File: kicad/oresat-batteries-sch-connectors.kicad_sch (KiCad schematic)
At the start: 13 parts, among them J1 J-SAMTEC-TFM-120-X1-XXX-D-RA, SW1 Omron D2F-L3-D (LEFT), SW2 Omron D2F-L3-D (RIGHT), SW3 OMRON D2F-L3-D (LEFT), SW4 OMRON D2F-L3-D (RIGHT)

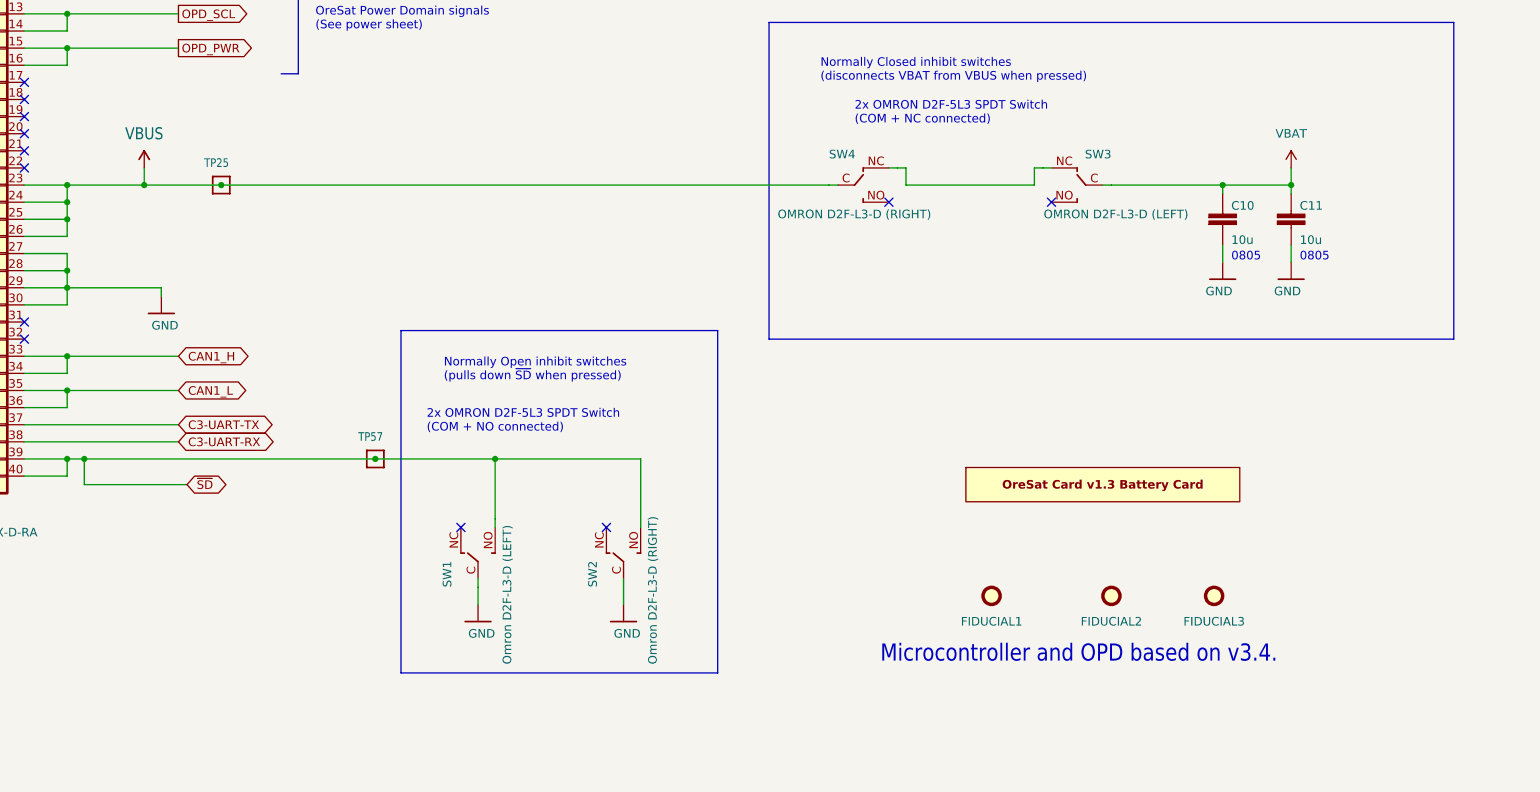
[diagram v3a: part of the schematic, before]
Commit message: Updated ground planes, battery foot prints, zones needs more work.
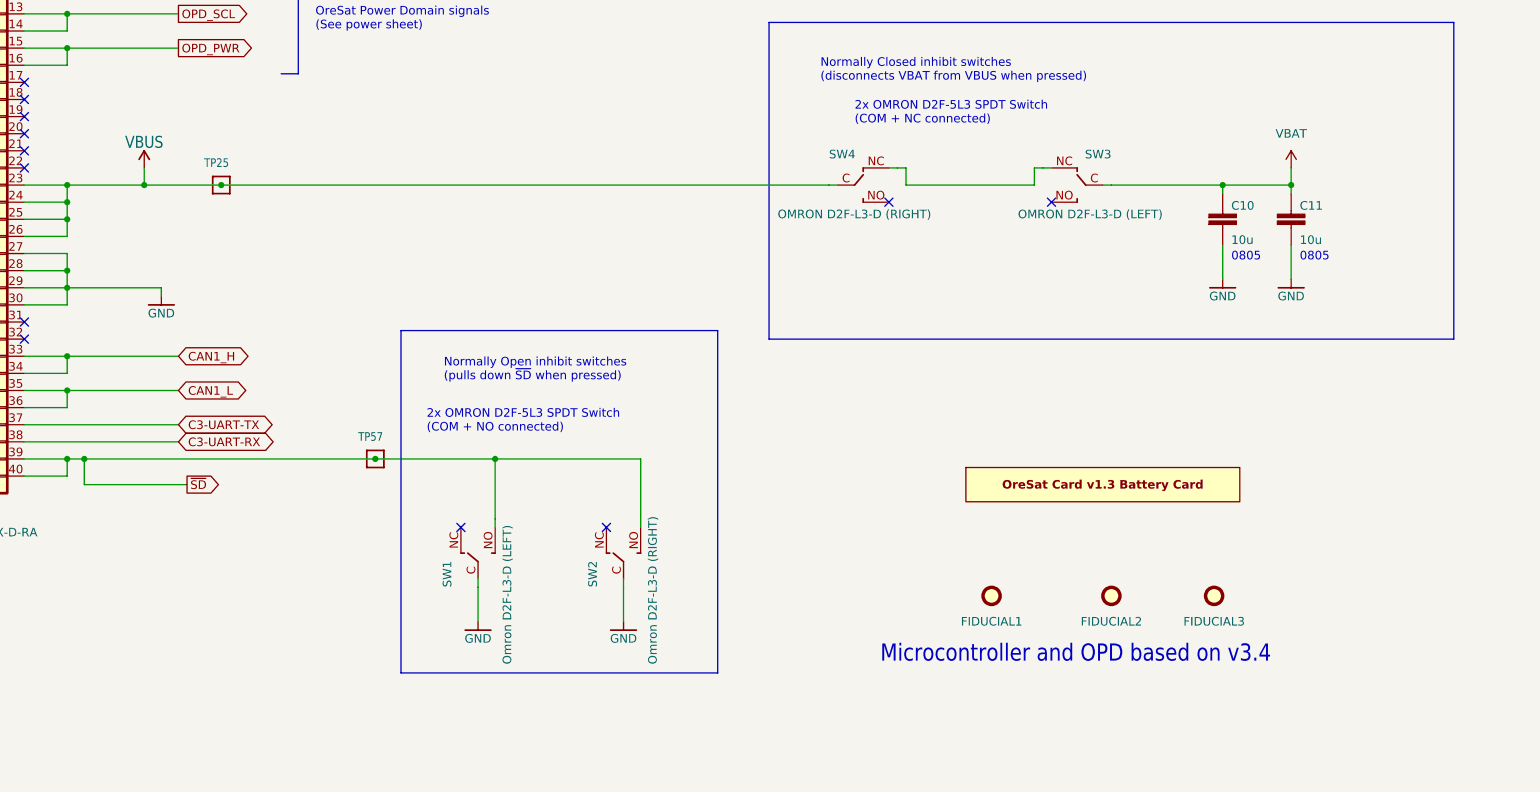
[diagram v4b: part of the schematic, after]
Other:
- note added: "Microcontroller and OPD based on v3.4"
- note removed: "Microcontroller and OPD based on v3.4."
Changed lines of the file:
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@@
     (stroke (width 0.1524) (type solid))
   )
-  (wire (pts (xy 290.83 110.49) (xy 290.83 113.03))
+  (wire (pts (xy 290.83 110.49) (xy 290.83 115.57))
     (stroke (width 0.1524) (type solid))
   )
@@
     (stroke (width 0.1524) (type solid))
   )
-  (wire (pts (xy 180.34 161.29) (xy 180.34 163.83))
+  (wire (pts (xy 180.34 161.29) (xy 180.34 166.37))
     (stroke (width 0.1524) (type solid))
   )
@@
     (stroke (width 0.1524) (type solid))
   )
-  (wire (pts (xy 201.93 163.83) (xy 201.93 161.29))
+  (wire (pts (xy 201.93 161.29) (xy 201.93 166.37))
     (stroke (width 0.1524) (type solid))
   )
@@
     (stroke (width 0.1524) (type solid))
   )
-  (wire (pts (xy 300.99 110.49) (xy 300.99 113.03))
+  (wire (pts (xy 300.99 110.49) (xy 300.99 115.57))
     (stroke (width 0.1524) (type solid))
   )
@@
     (effects (font (size 1.27 1.27)) (justify left bottom))
   )
-  (text "Microcontroller and OPD based on v3.4." (at 240.03 172.72 0)
+  (text "Microcontroller and OPD based on v3.4" (at 240.03 172.72 0)
     (effects (font (size 2.54 2.159)) (justify left bottom))
   )
@@
     )
   )
-  (global_label "~{SD}" (shape bidirectional) (at 137.16 146.05 0) (fields_autoplaced)
+  (global_label "~{SD}" (shape output) (at 137.16 146.05 0) (fields_autoplaced)
     (effects (font (size 1.27 1.27)) (justify left))
-    (property "Intersheetrefs" "${INTERSHEET_REFS}" (at 143.736 146.05 0)
+    (property "Intersheetrefs" "${INTERSHEET_REFS}" (at 142.6247 146.05 0)
       (effects (font (size 1.27 1.27)) (justify left))
     )
@@
     )
   )
-  (symbol (lib_id "oresat-batteries-eagle-import:supply1_GND") (at 133.35 120.65 0) (mirror y) (unit 1)
-    (in_bom yes) (on_board yes) (dnp no)
-    (property "Reference" "#GND01" (at 133.35 120.65 0)
-      (effects (font (size 1.27 1.27)) hide)
-    )
-    (property "Value" "GND" (at 135.89 123.19 0)
-      (effects (font (size 1.27 1.27)) (justify left bottom))
-    )
-    (property "Footprint" "" (at 133.35 120.65 0)
-      (effects (font (size 1.27 1.27)) hide)
-    )
-    (property "Datasheet" "" (at 133.35 120.65 0)
-      (effects (font (size 1.27 1.27)) hide)
-    )
-    (pin "1")
-    (instances
-      (project "oresat-batteries"
-        (path "/d5070776-2522-4f7b-9d31-10770161e48a/9be27716-7ec6-4c1f-ab95-233dfa83999d"
-          (reference "#GND01") (unit 1)
-        )
-      )
-    )
-  )
   (symbol (lib_id "oresat-misc:OMRON-D2F-L3-D-LEFT") (at 180.34 156.21 90) (unit 1)
     (in_bom yes) (on_board yes) (dnp no)
@@
     )
   )
-  (symbol (lib_id "oresat-batteries-eagle-import:supply1_GND") (at 300.99 115.57 0) (unit 1)
+  (symbol (lib_id "oresat-power:GND") (at 300.99 115.57 0) (unit 1)
     (in_bom yes) (on_board yes) (dnp no)
     (property "Reference" "#GND037" (at 300.99 115.57 0)
       (effects (font (size 1.27 1.27)) hide)
     )
-    (property "Value" "GND" (at 298.45 118.11 0)
-      (effects (font (size 1.27 1.27)) (justify left bottom))
-    )
-    (property "Footprint" "" (at 300.99 115.57 0)
-      (effects (font (size 1.27 1.27)) hide)
-    )
-    (property "Datasheet" "" (at 300.99 115.57 0)
+    (property "Value" "GND" (at 300.99 118.11 0) (do_not_autoplace)
+      (effects (font (size 1.27 1.27)))
+    )
+    (property "Footprint" "" (at 300.99 116.84 0)
+      (effects (font (size 1.27 1.27)) hide)
+    )
+    (property "Datasheet" "" (at 300.99 116.84 0)
       (effects (font (size 1.27 1.27)) hide)
     )
@@
       (effects (font (size 1.27 1.27)) (justify left bottom))
     )
-    (property "Value" "OMRON D2F-L3-D (LEFT)" (at 285.75 106.68 0)
+    (property "Value" "OMRON D2F-L3-D (LEFT)" (at 281.94 106.68 0)
       (effects (font (size 1.27 1.27)) (justify left bottom))
     )
@@
     )
   )
-  (symbol (lib_id "oresat-batteries-eagle-import:supply1_GND") (at 201.93 166.37 0) (mirror y) (unit 1)
+  (symbol (lib_id "oresat-power:GND") (at 201.93 166.37 0) (mirror y) (unit 1)
     (in_bom yes) (on_board yes) (dnp no)
     (property "Reference" "#GND073" (at 201.93 166.37 0)
       (effects (font (size 1.27 1.27)) hide)
     )
-    (property "Value" "GND" (at 204.47 168.91 0)
-      (effects (font (size 1.27 1.27)) (justify left bottom))
-    )
-    (property "Footprint" "" (at 201.93 166.37 0)
-      (effects (font (size 1.27 1.27)) hide)
-    )
-    (property "Datasheet" "" (at 201.93 166.37 0)
+    (property "Value" "GND" (at 201.93 168.91 0) (do_not_autoplace)
+      (effects (font (size 1.27 1.27)))
+    )
+    (property "Footprint" "" (at 201.93 167.64 0)
+      (effects (font (size 1.27 1.27)) hide)
+    )
+    (property "Datasheet" "" (at 201.93 167.64 0)
       (effects (font (size 1.27 1.27)) hide)
     )
@@
       (effects (font (size 1.27 1.27)) hide)
     )
-    (property "Value" "VBUS" (at 130.81 93.98 0)
+    (property "Value" "VBUS" (at 130.81 95.25 0)
       (effects (font (size 1.778 1.5113)))
     )
@@
     )
   )
-  (symbol (lib_id "oresat-batteries-eagle-import:supply1_GND") (at 180.34 166.37 0) (mirror y) (unit 1)
+  (symbol (lib_id "oresat-power:GND") (at 180.34 166.37 0) (mirror y) (unit 1)
     (in_bom yes) (on_board yes) (dnp no)
     (property "Reference" "#GND072" (at 180.34 166.37 0)
       (effects (font (size 1.27 1.27)) hide)
     )
-    (property "Value" "GND" (at 182.88 168.91 0)
-      (effects (font (size 1.27 1.27)) (justify left bottom))
-    )
-    (property "Footprint" "" (at 180.34 166.37 0)
-      (effects (font (size 1.27 1.27)) hide)
-    )
-    (property "Datasheet" "" (at 180.34 166.37 0)
+    (property "Value" "GND" (at 180.34 168.91 0) (do_not_autoplace)
+      (effects (font (size 1.27 1.27)))
+    )
+    (property "Footprint" "" (at 180.34 167.64 0)
+      (effects (font (size 1.27 1.27)) hide)
+    )
+    (property "Datasheet" "" (at 180.34 167.64 0)
       (effects (font (size 1.27 1.27)) hide)
     )
@@
     )
   )
-  (symbol (lib_id "oresat-batteries-eagle-import:supply1_GND") (at 290.83 115.57 0) (unit 1)
+  (symbol (lib_id "oresat-power:GND") (at 290.83 115.57 0) (unit 1)
     (in_bom yes) (on_board yes) (dnp no)
     (property "Reference" "#GND036" (at 290.83 115.57 0)
       (effects (font (size 1.27 1.27)) hide)
     )
-    (property "Value" "GND" (at 288.29 118.11 0)
-      (effects (font (size 1.27 1.27)) (justify left bottom))
-    )
-    (property "Footprint" "" (at 290.83 115.57 0)
-      (effects (font (size 1.27 1.27)) hide)
-    )
-    (property "Datasheet" "" (at 290.83 115.57 0)
+    (property "Value" "GND" (at 290.83 118.11 0) (do_not_autoplace)
+      (effects (font (size 1.27 1.27)))
+    )
+    (property "Footprint" "" (at 290.83 116.84 0)
+      (effects (font (size 1.27 1.27)) hide)
+    )
+    (property "Datasheet" "" (at 290.83 116.84 0)
       (effects (font (size 1.27 1.27)) hide)
     )
@@
         )
       )
+    )
+  )
+  (symbol (lib_name "GND_1") (lib_id "oresat-power:GND") (at 133.35 118.11 0) (unit 1)
+    (in_bom yes) (on_board yes) (dnp no) (fields_autoplaced)
+    (property "Reference" "#PWR03" (at 133.35 123.19 0)
+      (effects (font (size 1.27 1.27)) hide)
+    )
+    (property "Value" "GND" (at 133.35 120.65 0) (do_not_autoplace)
+      (effects (font (size 1.27 1.27)))
+    )
+    (property "Footprint" "" (at 133.35 119.38 0)
+      (effects (font (size 1.27 1.27)) hide)
+    )
+    (property "Datasheet" "" (at 133.35 119.38 0)
+      (effects (font (size 1.27 1.27)) hide)
+    )
+    (pin "1")
+    (instances
+      (project "oresat-batteries"
+        (path "/d5070776-2522-4f7b-9d31-10770161e48a/9be27716-7ec6-4c1f-ab95-233dfa83999d"
+          (reference "#PWR03") (unit 1)
+        )
+      )
